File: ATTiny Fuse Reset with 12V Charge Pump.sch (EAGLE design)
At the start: 34 parts, among them U2 ARDUINOR3-BPLACE

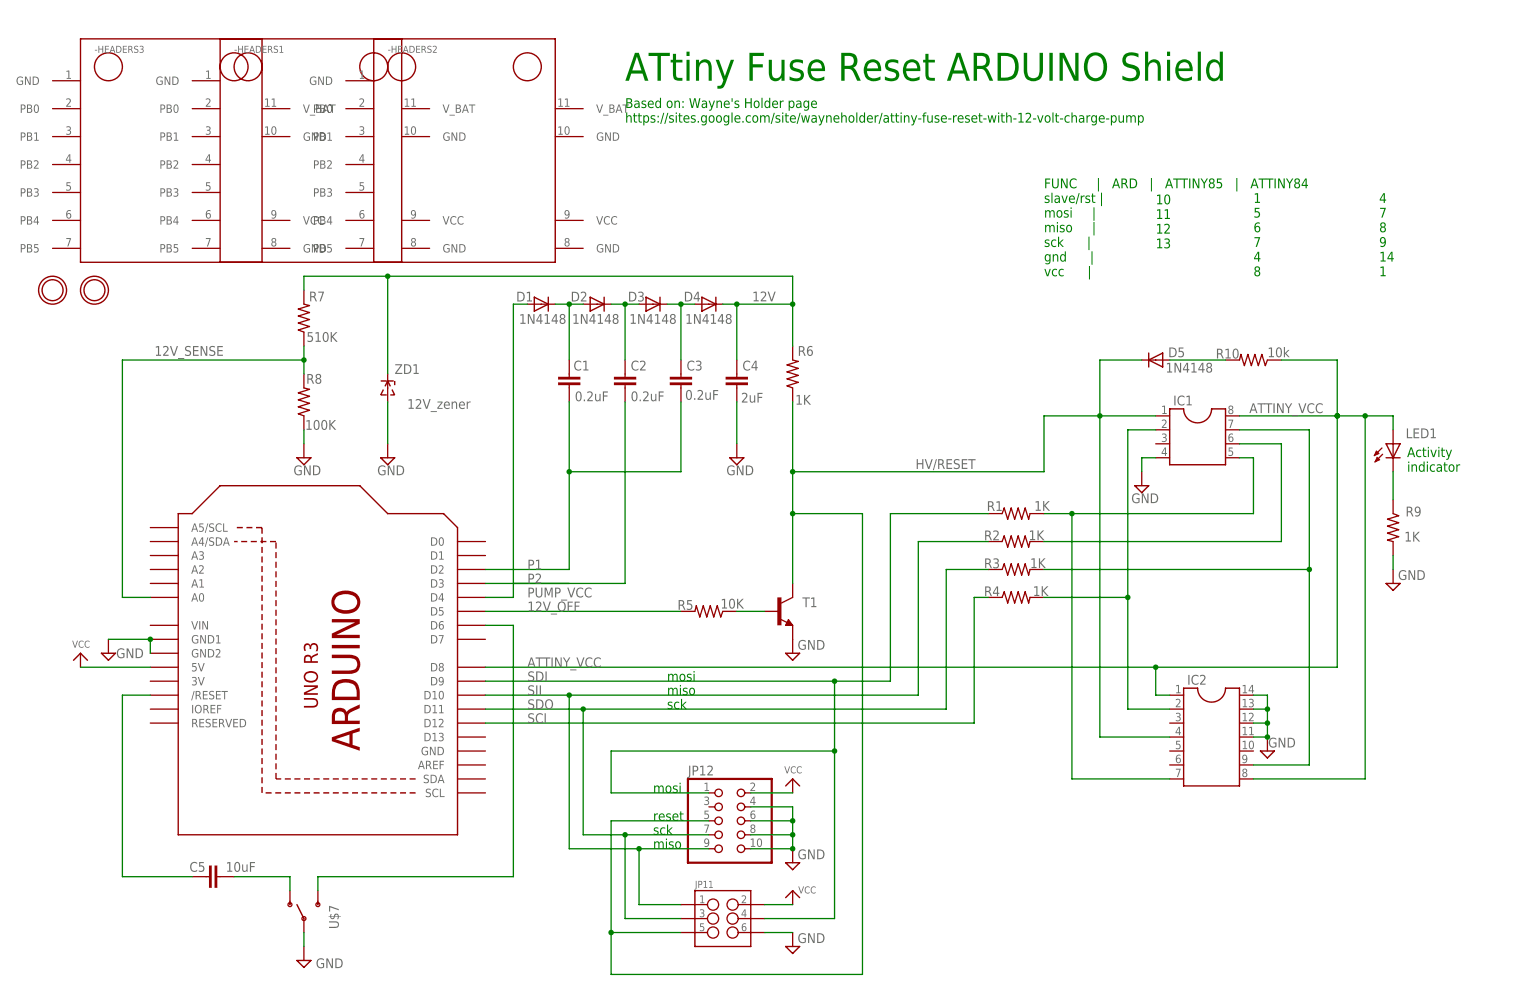
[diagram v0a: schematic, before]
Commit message: Changes in the schematic
MOSI, MISO, SCK and 12V_OFF are now connected to the correct pins of the
Arduino UNO
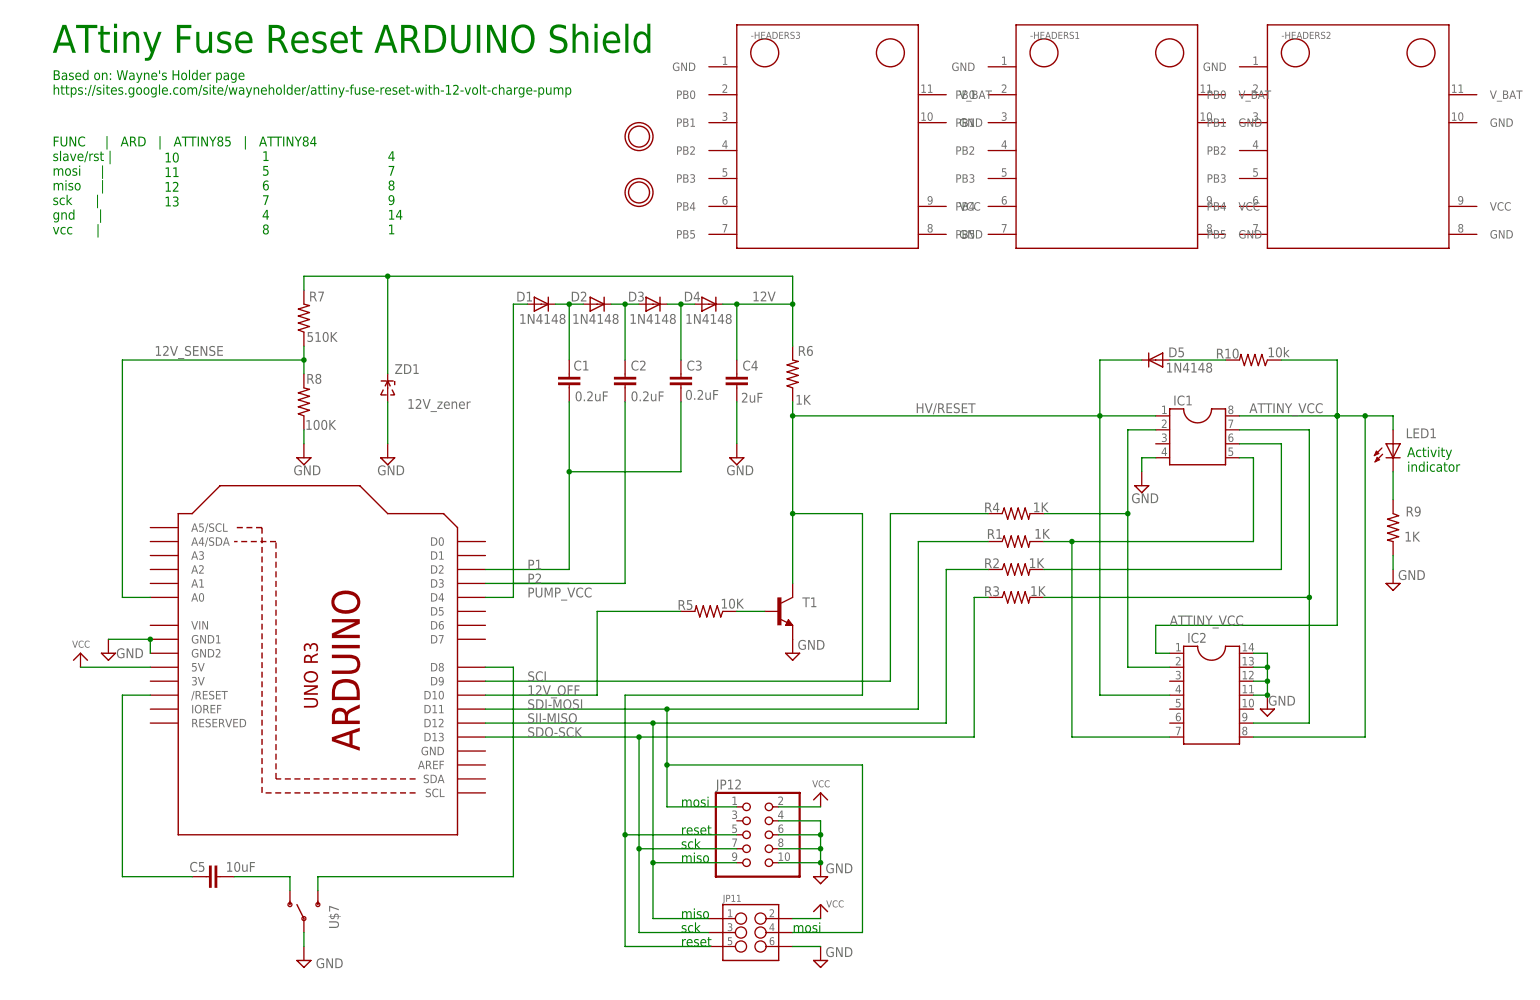
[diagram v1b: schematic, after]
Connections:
- removed net SDI: JP11.4, JP12.1, R1.1, U2.D9
- removed net SDO: JP11.3, JP12.7, R3.1, U2.D11
- removed net SII: JP11.1, JP12.9, R2.1, U2.D10
- new net SDI-MOSI: JP11.4, JP12.1, R1.1, U2.D11
- new net SDO-SCK: JP11.3, JP12.7, R3.1, U2.D13
- new net SII-MISO: JP11.1, JP12.9, R2.1, U2.D12
- net 12V_OFF: now also U2.D10; no longer U2.D5
- net ATTINY_VCC: no longer U2.D8
- net N$9: now also U2.D8; no longer U2.D6
- net SCI: now also U2.D9; no longer U2.D12
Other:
- moved on the sheet: -HEADERS1, -HEADERS2, -HEADERS3, IC2, JP11, JP12, R1, R2, R3, R4

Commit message: error correction: ATTINY_VCC wire was not connected
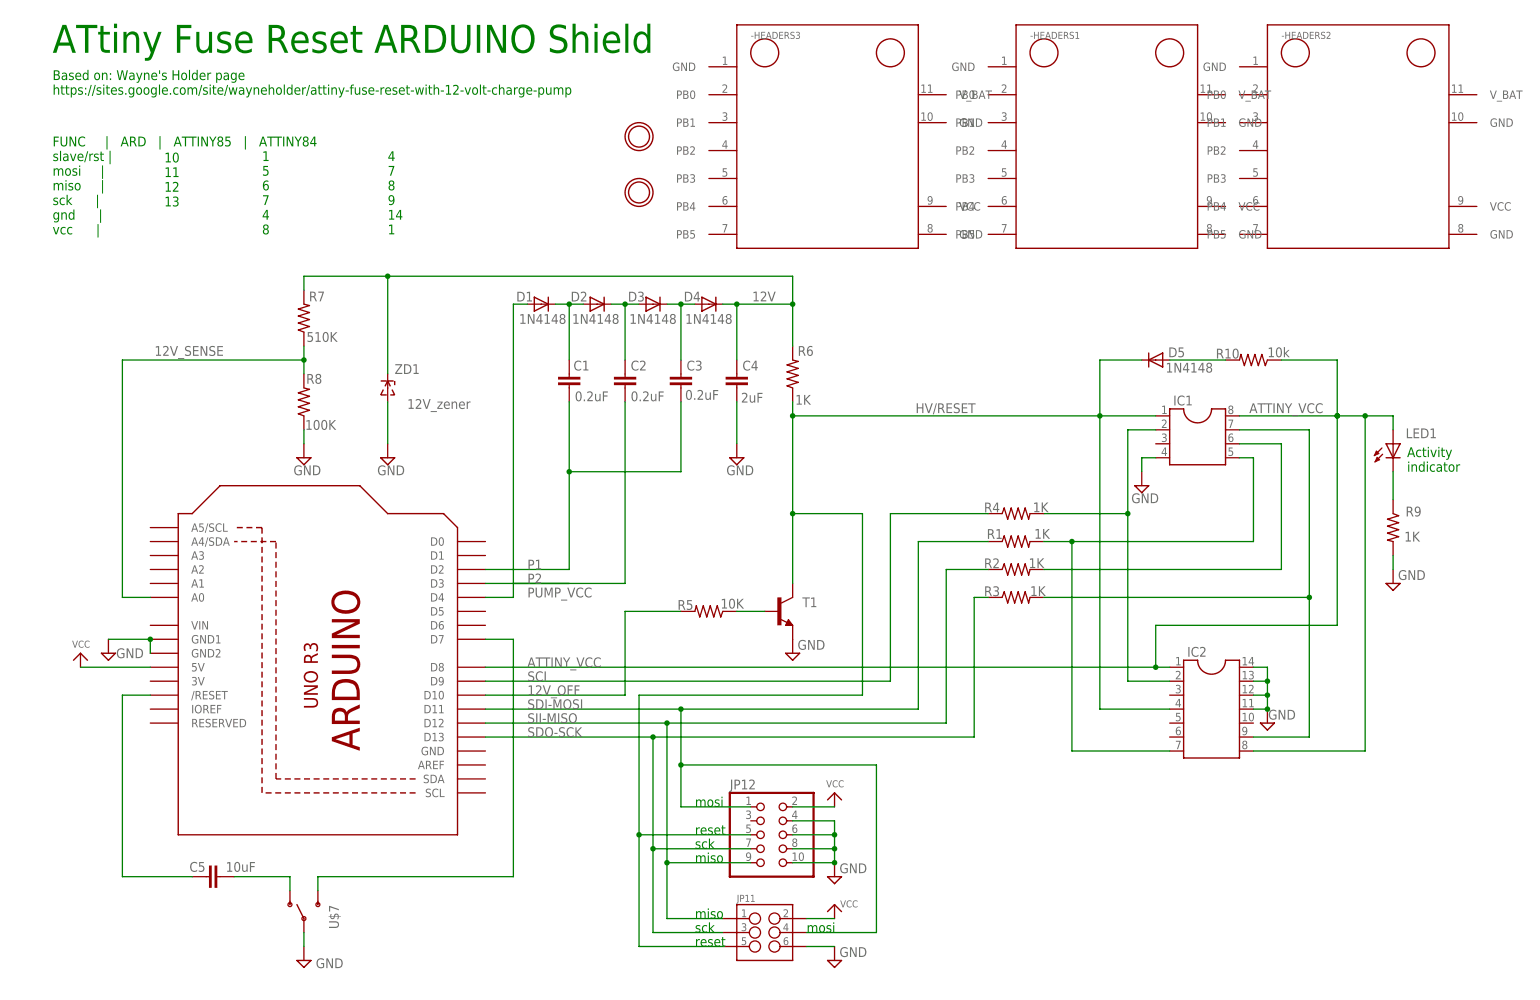
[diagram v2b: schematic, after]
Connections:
- net ATTINY_VCC: now also U2.D8
- net N$9: now also U2.D7; no longer U2.D8
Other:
- moved on the sheet: IC2, JP11, JP12

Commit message: Some more corrections
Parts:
- added R11: 1K, ATtami:RESISTOR0805-RES
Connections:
- removed net N$19: R5.1, T1.B
- new net N$1: R11.1, R5.1, T1.B
- net 12V_OFF: now also U2.D5; no longer U2.D10
- net GND: now also R11.2
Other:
- moved on the sheet: JP11, JP12, R5, R6, T1

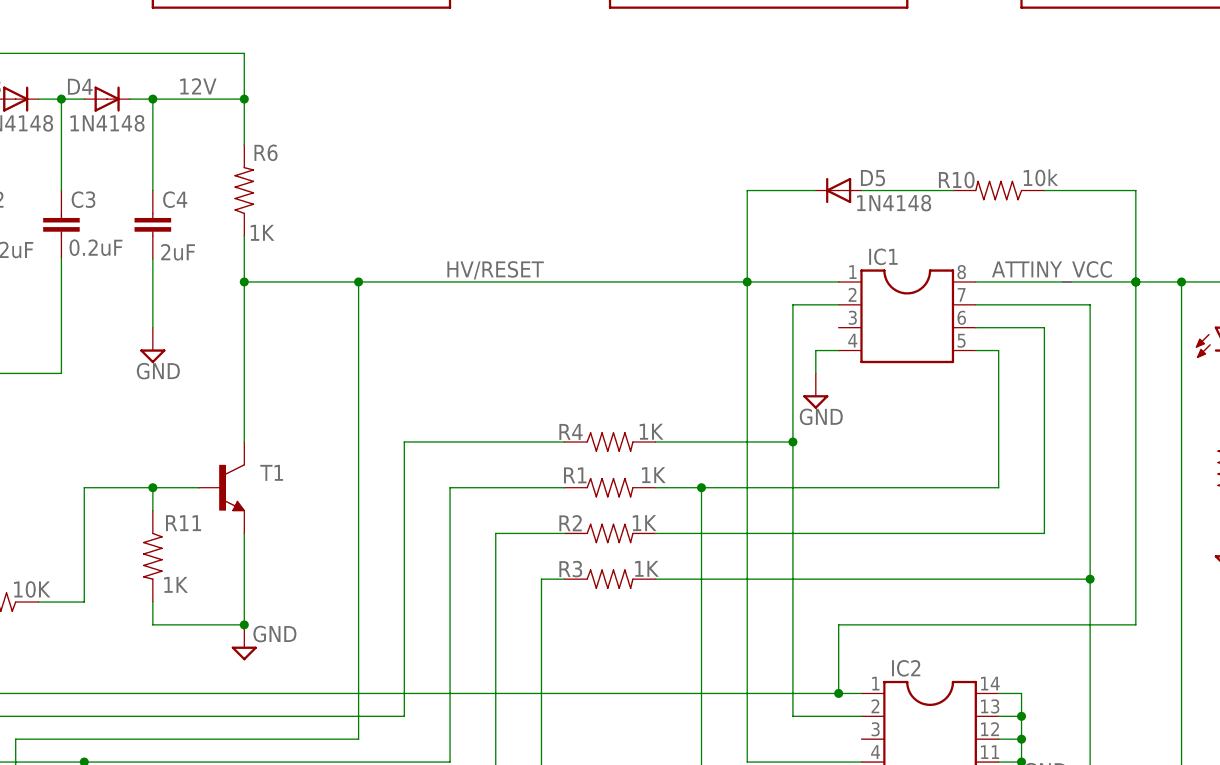
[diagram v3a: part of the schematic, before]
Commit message: R6, R10 and R11 values changed
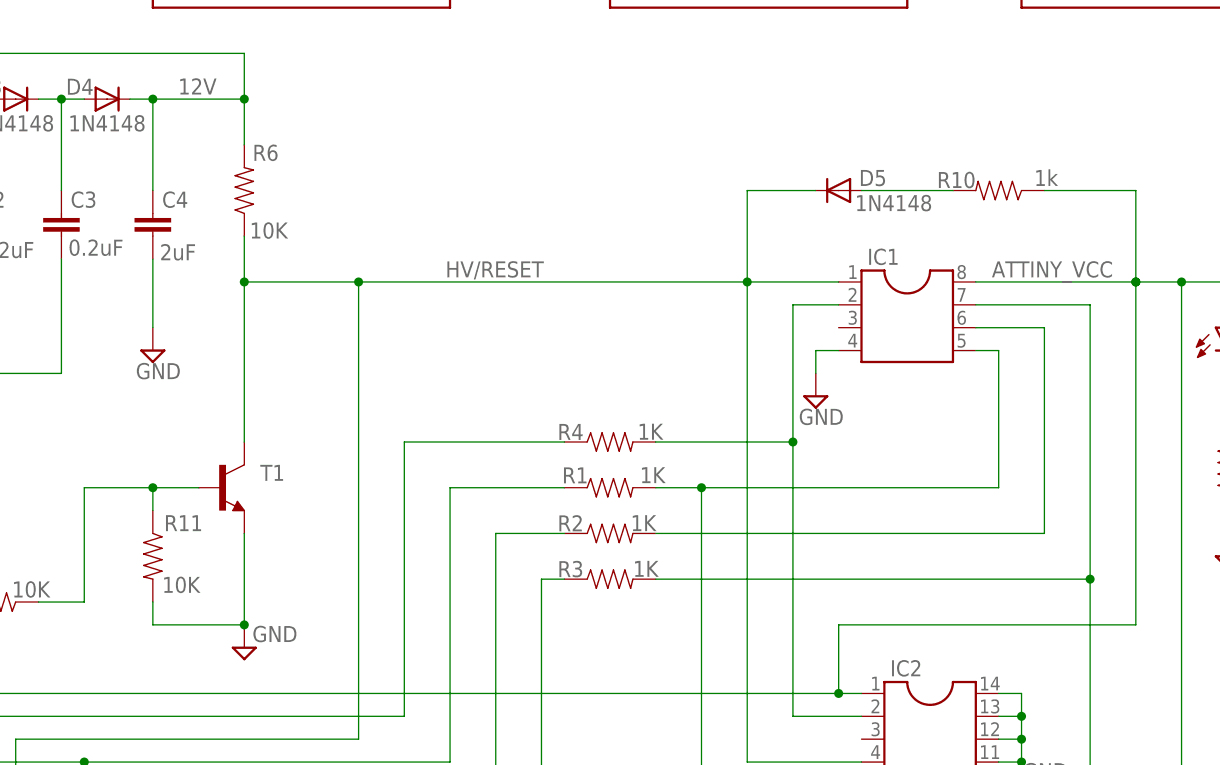
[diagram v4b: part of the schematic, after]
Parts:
- R10: value 10k -> 1k
- R11, R6: value 1K -> 10K
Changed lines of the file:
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@@
 <part name="R4" library="ATtami" deviceset="RESISTOR" device="0805-RES" value="1K"/>
 <part name="R5" library="ATtami" deviceset="RESISTOR" device="0805-RES" value="10K"/>
-<part name="R6" library="ATtami" deviceset="RESISTOR" device="0805-RES" value="1K"/>
+<part name="R6" library="ATtami" deviceset="RESISTOR" device="0805-RES" value="10K"/>
 <part name="R7" library="ATtami" deviceset="RESISTOR" device="0805-RES" value="510K"/>
 <part name="R8" library="ATtami" deviceset="RESISTOR" device="0805-RES" value="100K"/>
@@
 <part name="SUPPLY5" library="supply2" deviceset="GND" device=""/>
 <part name="LED1" library="ATtami" deviceset="LED" device="-0805"/>
-<part name="R10" library="ATtami" deviceset="RESISTOR" device="0805-RES" value="10k"/>
+<part name="R10" library="ATtami" deviceset="RESISTOR" device="0805-RES" value="1k"/>
 <part name="D5" library="ATtami" deviceset="SCHOTTKY-DIODE" device="SOD-323" value="1N4148"/>
 <part name="JP11" library="SparkFun-Connectors" deviceset="M03X2" device=""/>
@@
 <part name="-HEADERS2" library="ATtami" deviceset="ATTANI_BREAKOUT_PINS" device="NOHEAD"/>
 <part name="-HEADERS3" library="ATtami" deviceset="ATTANI_BREAKOUT_PINS" device=""/>
-<part name="R11" library="ATtami" deviceset="RESISTOR" device="0805-RES" value="1K"/>
+<part name="R11" library="ATtami" deviceset="RESISTOR" device="0805-RES" value="10K"/>
 </parts>
 <sheets>
@@
 <instance part="R6" gate="G$1" x="-180.34" y="116.84" smashed="yes" rot="R90">
 <attribute name="NAME" x="-176.5046" y="121.92" size="1.778" layer="95" rot="R180"/>
-<attribute name="VALUE" x="-177.038" y="113.03" size="1.778" layer="96" rot="R180"/>
+<attribute name="VALUE" x="-175.514" y="113.284" size="1.778" layer="96" rot="R180"/>
 </instance>
 <instance part="R7" gate="G$1" x="-269.24" y="124.46" smashed="yes" rot="R90">

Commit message: Changes in the schematic
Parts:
- added C6: 2uF, ATtami:CAP0805
- added R12: 10K, ATtami:RESISTOR0805-RES
- -HEADERS1: value (none) -> ATTami
- IC1: value (none) -> ATTinyx5/13
- IC2: value (none) -> ATTinyx4
- JP11: value (none) -> 6 pin ISP
- JP12: value (none) -> 10 pin ISP
- R6: value 10K -> 2.2K
- R9: value 1K -> 220R
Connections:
- removed net N$13: IC1.6, R2.2
- removed net N$14: IC1.2, IC2.2, R4.2
- removed net SDI-MOSI: JP11.4, JP12.1, R1.1, U2.D11
- new net N$21: R1.1, U2.D11
- new net N$7: R3.1, U2.D13
- new net SDI_MOSI: IC1.5, IC2.7, JP11.4, JP12.1, R1.2
- net ATTINY_VCC: now also C6.1; no longer IC2.8
- net GND: now also C6.2
- net N$2: now also R4.1, U2.D9; no longer IC1.5, IC2.7, R1.2
- net N$8: now also R2.1, U2.D12; no longer IC1.7, IC2.9, R3.2
- net N$9: now also R12.2
- net SCI: now also IC1.2, IC2.2, R4.2; no longer R4.1, U2.D9
- net SDO-SCK: now also IC1.7, IC2.9, R3.2; no longer R3.1, U2.D13
- net SII-MISO: now also IC1.6, IC2.8, R2.2; no longer R2.1, U2.D12
- net VCC: now also R12.1
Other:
- note added: "ATtiny Fuse Reset & ISP ARDUINO Shield"
- note removed: "1 5 6 7 4 8"
- note removed: "10 11 12 13"
- note removed: "4 7 8 9 14 1"
- note removed: "ATtiny Fuse Reset ARDUINO Shield"
- note removed: "FUNC | ARD | ATTINY85 | ATTINY84 slave/rst | mosi | miso | sck | gnd | vcc |"
- note removed: "miso"
- note removed: "mosi"
- note removed: "reset"
- note removed: "sck"
- moved on the sheet: -HEADERS1, -HEADERS2, -HEADERS3, C1, C2, C3, C4, C5, D1, D2, D3, D4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
